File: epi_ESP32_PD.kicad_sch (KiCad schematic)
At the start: 53 parts, among them J1 Conn_01x08, J2 USB_C_Receptacle_USB2.0, J3 Conn_01x08, J4 Conn_01x02, J5 Conn_01x06, Q1 Q_PMOS_GDS, Q2 Q_NMOS_GDS, Q3 Q_NMOS_GDS, Q4 Q_NMOS_GDS, Q5 Q_NMOS_GDS, Q6 Q_NMOS_GDS, SW1 SW_MEC_5G, SW2 SW_MEC_5G, U1 ESP32-C3, U2 MIC5219-5.0YM5, U4 MIC5219-3.3YM5, Y1 Crystal

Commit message: designed
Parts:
- removed AE1: Antenna, DIY:2450AT14A0100001T, symbol Device:Antenna
- removed C9: 1µF, Capacitor_SMD:C_0402_1005Metric, symbol Device:C_Small
- removed J5: Conn_01x06, Connector_PinHeader_1.27mm:PinHeader_1x06_P1.27mm_Horizontal, symbol Connector_Generic:Conn_01x06
- removed RV1, RV4: Varistor, Resistor_SMD:R_0402_1005Metric, symbol Device:Polyfuse_Small
- removed U4: MIC5219-3.3YM5, Package_TO_SOT_SMD:SOT-23-5, symbol Regulator_Linear:MIC5219-3.3YM5
- added C15: 100nF, Capacitor_SMD:C_0402_1005Metric, symbol Device:C_Small
- added C16, C17: 22µF, Capacitor_SMD:C_0805_2012Metric, symbol Device:C_Small
- added J6: Conn_Coaxial_Small, Connector_Coaxial:U.FL_Molex_MCRF_73412-0110_Vertical, symbol Connector:Conn_Coaxial_Small
- added J7: Conn_02x03, Connector_PinHeader_2.54mm:PinHeader_2x03_P2.54mm_Horizontal, symbol Connector_Generic:Conn_02x03_Odd_Even
- added J8: Conn_01x03, Connector_PinHeader_2.54mm:PinHeader_1x03_P2.54mm_Vertical, symbol Connector_Generic:Conn_01x03
- added L2: TBD, Inductor_SMD:L_Abracon_ASPI-0425, symbol Device:L_Small
- added R13, R14, R15: 10K, Resistor_SMD:R_0402_1005Metric, symbol Device:R_Small
- added U5: AP63205WU, Package_TO_SOT_SMD:TSOT-23-6, symbol Regulator_Switching:AP63203WU
- C10: value 22µF -> 10µF; footprint Capacitor_SMD:C_0603_1608Metric -> Capacitor_SMD:C_0805_2012Metric
- J1, J3: footprint Connector_PinHeader_1.27mm:PinHeader_1x08_P1.27mm_Vertical -> Connector_PinHeader_2.54mm:PinHeader_1x08_P2.54mm_Vertical
- U2: value MIC5219-5.0YM5 -> MIC5219-3.3YM5
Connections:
- net +3.3V: now also C14.2, U2.5 (OUT), J8.1 (Pin_1), R13.2, R14.2; no longer C10.2
- net +5V: now also C13.2, U2.1 (IN), U2.3 (EN), C16.2, C17.2, L2.2, U5.1 (FB); no longer C14.2, U2.5 (OUT)
- net B: now also J7.3 (Pin_3)
- net D+: now also RV2.1; no longer RV2.2
- net D-: now also RV3.1; no longer RV3.2
- net GND: now also RV2.2, RV3.2, C16.1, C17.1, J6.2 (Ext), J7.2 (Pin_2), J8.3 (Pin_3), R15.1, U5.4 (GND); no longer RV2.1, RV3.1
- net IO0: now also J8.2 (Pin_2)
- net IO2_5V: now also J7.4 (Pin_4)
- net IO3_5V: now also J7.6 (Pin_6)
- net IO6: now also R13.1
- net IO7: now also R14.1
- net VOUT: now also J7.1 (Pin_1)
- net W: now also J7.5 (Pin_5)
- net at JP3.1 (A), U3.9 (CFG1): now also R15.2
- net at L1.2: now also J6.1 (In)
- net VCC renamed VIN
- net VIN: now also C10.2, U5.2 (EN), U5.3 (IN); no longer C13.2, U2.1 (IN), U2.3 (EN)
- new net: C15.1, U5.6 (BST)
- new net buck: C15.2, L2.1, U5.5 (SW)
- no-connect marks 11 -> 10
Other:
- moved on the sheet: C1, C10, C11, C12, C13, C14, C2, C3, C4, C5, C6, C7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

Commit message: made it pretty
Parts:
- added JP4: Jumper, Jumper:SolderJumper-2_P1.3mm_Open_RoundedPad1.0x1.5mm, symbol Jumper:Jumper_2_Small_Open
- J2: footprint diy:USB-C MC-314C-4P16_V2 (2023_01_13 17_48_46 UTC) -> Connector_USB:USB_C_Receptacle_G-Switch_GT-USB-7010ASV
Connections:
- net +5V: now also JP4.1 (A)
- net VIN: now also JP4.2 (B)
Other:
- moved on the sheet: C10, C15, C16, C17, L2, U5

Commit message: finishing touches
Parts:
- removed C8: 1µF, Capacitor_SMD:C_0805_2012Metric, symbol Device:C_Small
- removed J4: Conn_01x02, Connector_PinHeader_2.54mm:PinHeader_1x02_P2.54mm_Vertical, symbol Connector_Generic:Conn_01x02
- added D1: D_Small, Diode_SMD:D_SOD-128, symbol Device:D_Small
- added J4: Conn_01x01, TestPoint:TestPoint_Pad_3.0x3.0mm, symbol Connector_Generic:Conn_01x01
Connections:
- net +5V: now also JP1.1 (A), JP2.1 (A), JP3.2 (B), R1.1, U3.1 (VDD)
- net GND: now also J4.1 (Pin_1)
- net VIN: now also D1.1 (K); no longer J2.A4 (VBUS), J2.A9 (VBUS), J2.B4 (VBUS), J2.B9 (VBUS), JP1.1 (A), JP2.1 (A), JP3.2 (B), R1.2, R7.1
- new net PD: D1.2 (A), J2.A4 (VBUS), J2.A9 (VBUS), J2.B4 (VBUS), J2.B9 (VBUS), R1.2, R7.1
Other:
- note added: "Connectors"
- note added: "High-power control"
- note added: "IO10 dedicated to switching the entire high-voltage output"
- note added: "Level shifters"
- note added: "MCU"
- note added: "Power"
- note added: "USB"
- note added: "Utility switches"
- note added: "VIN is represented by a bare patch on the board"
- moved on the sheet: C1, C10, C11, C12, C13, C14, C15, C16, C17, C2, C3, C4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

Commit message: little fix
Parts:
- added C8: 1µF, Capacitor_SMD:C_0402_1005Metric, symbol Device:C_Small
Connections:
- net +3.3V: now also JP1.1 (A), JP2.1 (A), JP3.2 (B), R1.1, U3.1 (VDD), C8.2
- net +5V: no longer JP1.1 (A), JP2.1 (A), JP3.2 (B), R1.1, U3.1 (VDD)
- net GND: now also C8.1

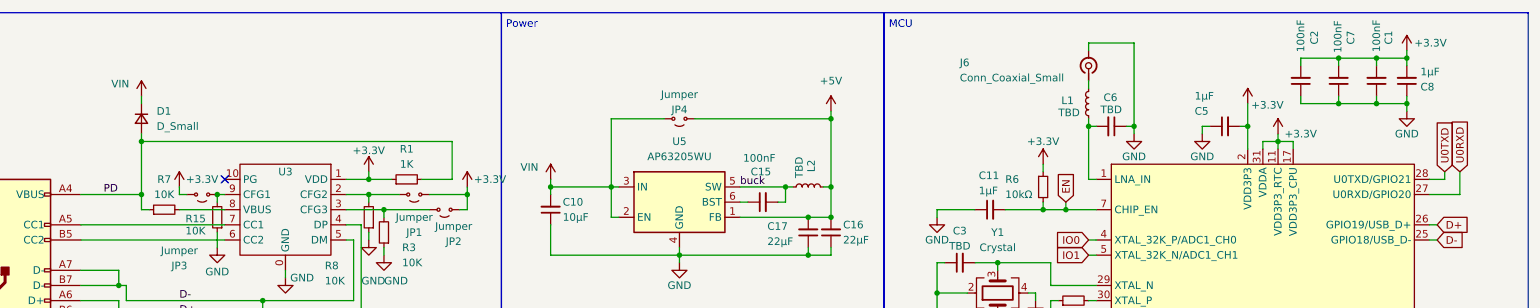
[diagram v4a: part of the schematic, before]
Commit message: added a couple debugging jumpers
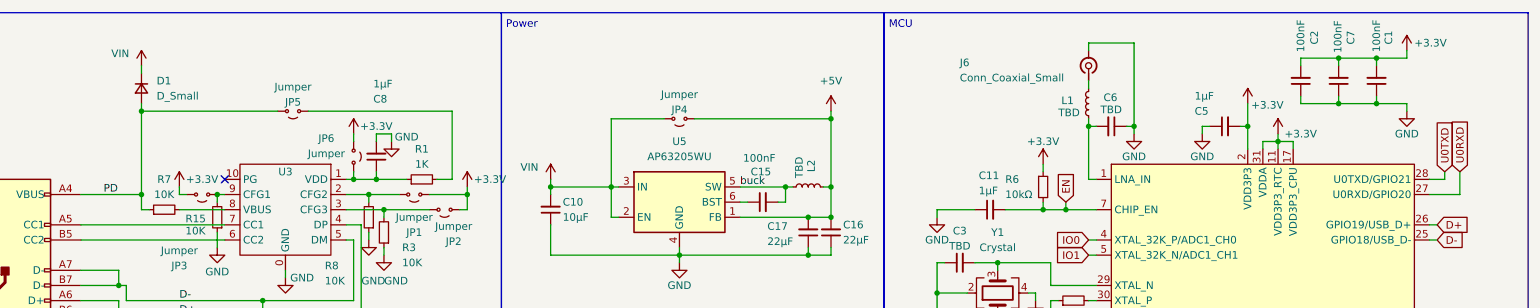
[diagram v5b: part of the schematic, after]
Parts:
- added JP5, JP6: Jumper, Jumper:SolderJumper-2_P1.3mm_Bridged_RoundedPad1.0x1.5mm, symbol Jumper:Jumper_2_Small_Open
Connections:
- net +3.3V: now also JP6.1 (A); no longer C8.2, R1.1, U3.1 (VDD)
- net GND: now also C8.2; no longer C8.1
- net PD: now also JP5.2 (B); no longer R1.2
- new net: C8.1, JP6.2 (B), R1.1, U3.1 (VDD)
- new net: JP5.1 (A), R1.2
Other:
- moved on the sheet: C8, D1, R1

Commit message: mix
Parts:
- added D2: D_Zener, Diode_SMD:D_SOD-323, symbol Device:D_Zener_Small
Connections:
- net GND: now also D2.2 (A)
- net at C8.1, JP6.2 (B), R1.1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: now also D2.1 (K)
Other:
- moved on the sheet: C10, C13, C14, C15, C16, C17, JP4, L2, R1, U2, U5

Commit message: revision
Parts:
- removed C12, C5: 1µF, Capacitor_SMD:C_0402_1005Metric, symbol Device:C_Small
- removed C14: 22µF, Capacitor_SMD:C_0603_1608Metric, symbol Device:C_Small
- removed C2, C7: 100nF, Capacitor_SMD:C_0402_1005Metric, symbol Device:C_Small
- removed C3, C4, C6: TBD, Capacitor_SMD:C_0402_1005Metric, symbol Device:C_Small
- removed D2: D_Zener, Diode_SMD:D_SOD-323, symbol Device:D_Zener_Small
- removed J3: Conn_01x08, Connector_PinHeader_2.54mm:PinHeader_1x08_P2.54mm_Vertical, symbol Connector_Generic:Conn_01x08
- removed J6: Conn_Coaxial_Small, Connector_Coaxial:U.FL_Molex_MCRF_73412-0110_Vertical, symbol Connector:Conn_Coaxial_Small
- removed JP5, JP6: Jumper, Jumper:SolderJumper-2_P1.3mm_Bridged_RoundedPad1.0x1.5mm, symbol Jumper:Jumper_2_Small_Open
- removed L1: TBD, Resistor_SMD:R_0402_1005Metric, symbol Device:L_Small
- removed Q1: Q_PMOS_GDS, Package_TO_SOT_SMD:SOT-23-3, symbol Device:Q_PMOS_GDS
- removed Q2, Q3, Q4, Q5, Q6: Q_NMOS_GDS, Package_TO_SOT_SMD:SOT-23-3, symbol Device:Q_NMOS_GDS
- removed R2: 22Ω, Resistor_SMD:R_0402_1005Metric, symbol Device:R_Small
- removed R4, R5: 10K, Resistor_SMD:R_0402_1005Metric, symbol Device:R_Small
- removed RV2: Varistor, Resistor_SMD:R_0402_1005Metric, symbol Device:Polyfuse_Small
- removed SW1: SW_MEC_5G, DIY:R-668048, symbol Switch:SW_MEC_5G
- removed U1: ESP32-C3, Package_DFN_QFN:QFN-32-1EP_5x5mm_P0.5mm_EP3.45x3.45mm, symbol PCM_Espressif:ESP32-C3
- removed Y1: Crystal, Crystal:Crystal_SMD_2016-4Pin_2.0x1.6mm, symbol Device:Crystal_GND24
- added J5: Conn_01x09, Connector_PinHeader_2.54mm:PinHeader_1x09_P2.54mm_Vertical, symbol Connector_Generic:Conn_01x09
- added Q1, Q2, Q3, Q4: Q_NMOS_GSD, Package_TO_SOT_SMD:SOT-23, symbol Device:Q_NMOS_GSD
- added U1: ESP32-C3-MINI-1, PCM_Espressif:ESP32-C3-MINI-1, symbol PCM_Espressif:ESP32-C3-MINI-1
- C1: value 100nF -> 1µF
- R1: value 1K -> TBD
- R15, R3, R8: value 10K -> 1K
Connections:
- net VOUT is gone; now on net +5V: J7.1 (Pin_1)
- net +3.3V: now also C8.1, R1.1, U3.1 (VDD), J5.1 (Pin_1), Q1.1 (G), Q2.1 (G), U1.3 (3V3); no longer R13.2, R14.2
- net +5V: now also J5.3 (Pin_3)
- net B: now also J7.4 (Pin_4), Q4.3 (D); no longer J7.3 (Pin_3)
- net BOOT: now also J5.6 (Pin_6), U1.23 (GPIO9)
- net D+: now also U1.27 (GPIO19/USB_D+); no longer U3.4 (DP)
- net D-: now also U1.26 (GPIO18/USB_D-); no longer RV3.1, U3.5 (DM)
- net EN: now also J5.4 (Pin_4), U1.8 (EN/CHIP_PU)
- net GND: now also R13.1, R14.1, J5.2 (Pin_2), Q3.2 (S), Q4.2 (S), U1.1 (GND), U1.11 (GND), U1.14 (GND), U1.2 (GND), U1.36 (GND), U1.37 (GND), U1.38 (GND), U1.39 (GND), U1.40 (GND), U1.41 (GND), U1.42 (GND), U1.43 (GND), U1.44 (GND), U1.45 (GND), U1.46 (GND), U1.47 (GND), U1.48 (GND), U1.49 (GND), U1.50 (GND), U1.51 (GND), U1.52 (GND), U1.53 (GND)
- net IO0: now also U1.12 (GPIO0/ADC1_CH0/XTAL_32K_P)
- net IO1: now also U1.13 (GPIO1/ADC1_CH1/XTAL_32K_N)
- net IO10: now also J5.5 (Pin_5), U1.16 (GPIO10)
- net IO2: now also Q1.2 (S), U1.5 (GPIO2/ADC1_CH2)
- net IO2_5V: now also J7.3 (Pin_3), Q1.3 (D); no longer J7.4 (Pin_4)
- net IO3: now also Q2.2 (S), U1.6 (GPIO3/ADC1_CH3)
- net IO3_5V: now also J7.5 (Pin_5), Q2.3 (D); no longer J7.6 (Pin_6)
- net IO4: now also U1.18 (GPIO4/ADC1_CH4)
- net IO5: now also U1.19 (GPIO5/ADC2_CH0)
- net IO6: now also R13.2, J5.9 (Pin_9), Q4.1 (G), U1.20 (GPIO6); no longer R13.1
- net IO7: now also R14.2, J5.8 (Pin_8), Q3.1 (G), U1.21 (GPIO7); no longer R14.1
- net IO8: now also J5.7 (Pin_7), U1.22 (GPIO8)
- net PD: now also R1.2, RV3.1
- net U0RXD: now also U1.30 (GPIO20/U0RXD)
- net U0TXD: now also U1.31 (GPIO21/U0TXD)
- net VIN: now also J7.0
- net W: now also J7.6 (Pin_6), Q3.3 (D); no longer J7.5 (Pin_5)
- no-connect marks 10 -> 6
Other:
- note removed: "IO10 dedicated to switching the entire high-voltage output"
- moved on the sheet: C11, C8, D1, J2, JP1, JP2, JP3, R13, R14, R15, R3, R6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
